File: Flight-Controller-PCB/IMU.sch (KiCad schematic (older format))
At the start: 13 parts, among them Q1 BSS138, Q2 BSS138, U2 ICM-20689

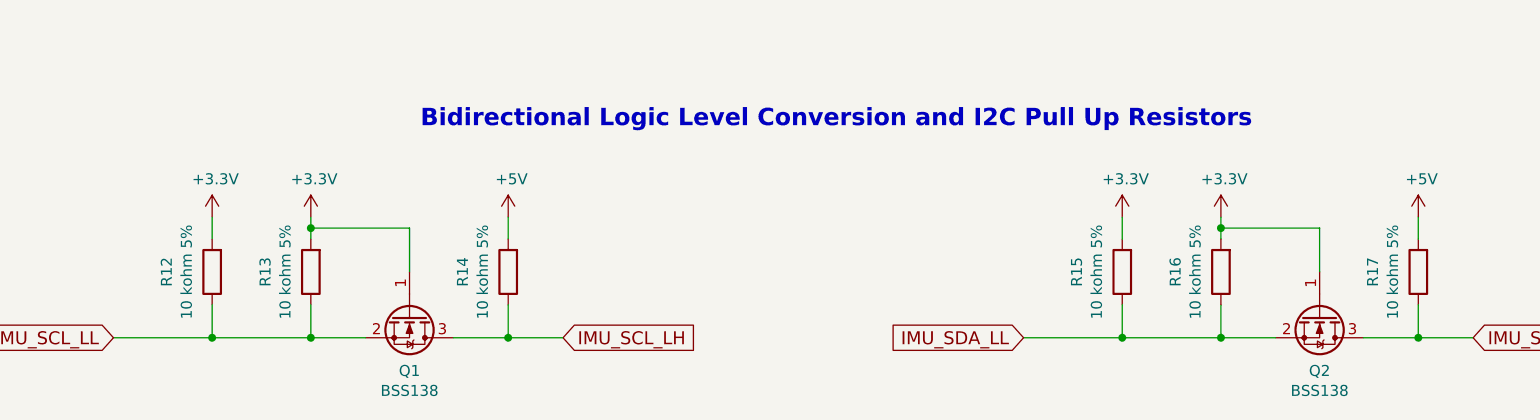
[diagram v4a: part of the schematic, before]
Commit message: Main page and IMU reviewed and passed
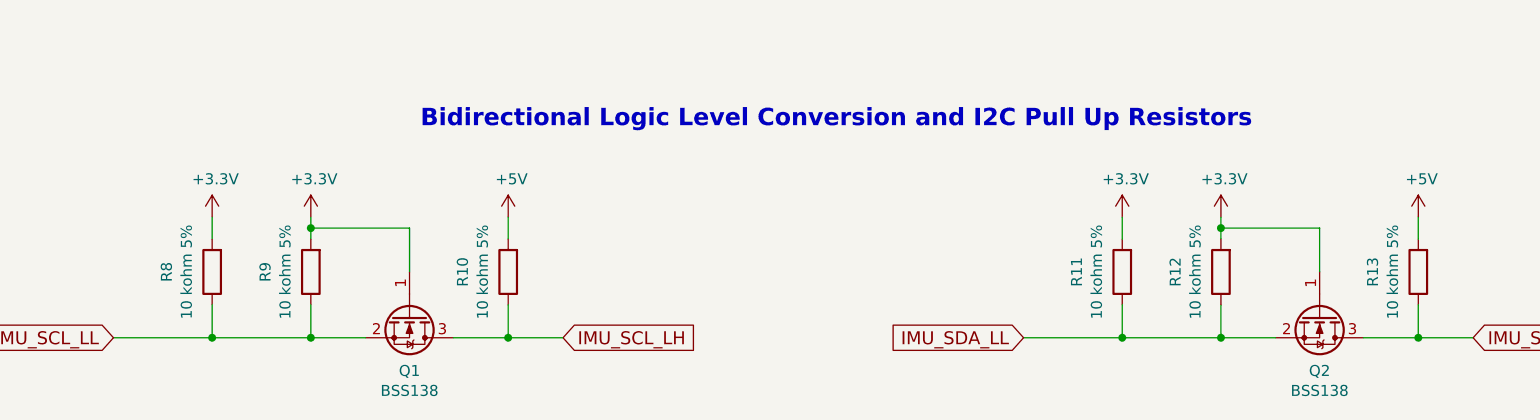
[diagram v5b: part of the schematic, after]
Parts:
- renumbered R14 to R10, R15 to R11, R16 to R12, R17 to R13, R12 to R8, R13 to R9
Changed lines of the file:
@@
 Sheet 2 3
 Title "Six Degree of Freedom (DOF) Inertial Measurement Unit (IMU)"
-Date "2020-12-21"
+Date "2021-01-01"
 Rev "A"
-Comp ""
+Comp "Mark Sherstan"
 Comment1 ""
 Comment2 ""
@@
 IMU_SCL_LL
 $Comp
-L power:+3.3V #PWR030
+L power:+3.3V #PWR034
 U 1 1 5FD9D00C
 P 2800 4700
-AR Path="/5FD99B6C/5FD9D00C" Ref="#PWR030"  Part="1"
+AR Path="/5FD99B6C/5FD9D00C" Ref="#PWR034"  Part="1"
 AR Path="/5FD9E07D/5FD9D00C" Ref="#PWR?"  Part="1"
-F 0 "#PWR030" H 2800 4550 50  0001 C CNN
+F 0 "#PWR034" H 2800 4550 50  0001 C CNN
 F 1 "+3.3V" H 2815 4873 50  0000 C CNN
 F 2 "" H 2800 4700 50  0001 C CNN
@@
 	5050 2800 4750 2800
 $Comp
-L power:GND #PWR035
+L power:GND #PWR039
 U 1 1 5FD9CFF8
 P 4750 3050
-AR Path="/5FD99B6C/5FD9CFF8" Ref="#PWR035"  Part="1"
+AR Path="/5FD99B6C/5FD9CFF8" Ref="#PWR039"  Part="1"
 AR Path="/5FD9E07D/5FD9CFF8" Ref="#PWR?"  Part="1"
-F 0 "#PWR035" H 4750 2800 50  0001 C CNN
+F 0 "#PWR039" H 4750 2800 50  0001 C CNN
 F 1 "GND" H 4755 2877 50  0000 C CNN
 F 2 "" H 4750 3050 50  0001 C CNN
@@
 	3300 2500 3300 3050
 $Comp
-L power:GND #PWR032
+L power:GND #PWR036
 U 1 1 5FD9CFEF
 P 3300 3050
-AR Path="/5FD99B6C/5FD9CFEF" Ref="#PWR032"  Part="1"
+AR Path="/5FD99B6C/5FD9CFEF" Ref="#PWR036"  Part="1"
 AR Path="/5FD9E07D/5FD9CFEF" Ref="#PWR?"  Part="1"
-F 0 "#PWR032" H 3300 2800 50  0001 C CNN
+F 0 "#PWR036" H 3300 2800 50  0001 C CNN
 F 1 "GND" H 3305 2877 50  0000 C CNN
 F 2 "" H 3300 3050 50  0001 C CNN
@@
 	3700 3050 3700 2950
 $Comp
-L power:GND #PWR033
+L power:GND #PWR037
 U 1 1 5FD9CFE8
 P 3700 3050
-AR Path="/5FD99B6C/5FD9CFE8" Ref="#PWR033"  Part="1"
+AR Path="/5FD99B6C/5FD9CFE8" Ref="#PWR037"  Part="1"
 AR Path="/5FD9E07D/5FD9CFE8" Ref="#PWR?"  Part="1"
-F 0 "#PWR033" H 3700 2800 50  0001 C CNN
+F 0 "#PWR037" H 3700 2800 50  0001 C CNN
 F 1 "GND" H 3705 2877 50  0000 C CNN
 F 2 "" H 3700 3050 50  0001 C CNN
@@
 	6050 2500 7050 2500
 $Comp
-L power:GND #PWR041
+L power:GND #PWR045
 U 1 1 5FD9CFD9
 P 8100 3000
-AR Path="/5FD99B6C/5FD9CFD9" Ref="#PWR041"  Part="1"
+AR Path="/5FD99B6C/5FD9CFD9" Ref="#PWR045"  Part="1"
 AR Path="/5FD9E07D/5FD9CFD9" Ref="#PWR?"  Part="1"
-F 0 "#PWR041" H 8100 2750 50  0001 C CNN
+F 0 "#PWR045" H 8100 2750 50  0001 C CNN
 F 1 "GND" H 8105 2827 50  0000 C CNN
 F 2 "" H 8100 3000 50  0001 C CNN
@@
 $EndComp
 $Comp
-L power:GND #PWR038
+L power:GND #PWR042
 U 1 1 5FD9CFD3
 P 7050 3000
-AR Path="/5FD99B6C/5FD9CFD3" Ref="#PWR038"  Part="1"
+AR Path="/5FD99B6C/5FD9CFD3" Ref="#PWR042"  Part="1"
 AR Path="/5FD9E07D/5FD9CFD3" Ref="#PWR?"  Part="1"
-F 0 "#PWR038" H 7050 2750 50  0001 C CNN
+F 0 "#PWR042" H 7050 2750 50  0001 C CNN
 F 1 "GND" H 7055 2827 50  0000 C CNN
 F 2 "" H 7050 3000 50  0001 C CNN
@@
 	6050 2350 6150 2350
 $Comp
-L power:+3.3V #PWR040
+L power:+3.3V #PWR044
 U 1 1 5FD9CFC9
 P 8100 2400
-AR Path="/5FD99B6C/5FD9CFC9" Ref="#PWR040"  Part="1"
+AR Path="/5FD99B6C/5FD9CFC9" Ref="#PWR044"  Part="1"
 AR Path="/5FD9E07D/5FD9CFC9" Ref="#PWR?"  Part="1"
-F 0 "#PWR040" H 8100 2250 50  0001 C CNN
+F 0 "#PWR044" H 8100 2250 50  0001 C CNN
 F 1 "+3.3V" H 8115 2573 50  0000 C CNN
 F 2 "" H 8100 2400 50  0001 C CNN
@@
 	2300 2250 2300 2350
 $Comp
-L power:GND #PWR029
+L power:GND #PWR033
 U 1 1 5FD9CFBF
 P 2300 2850
-AR Path="/5FD99B6C/5FD9CFBF" Ref="#PWR029"  Part="1"
+AR Path="/5FD99B6C/5FD9CFBF" Ref="#PWR033"  Part="1"
 AR Path="/5FD9E07D/5FD9CFBF" Ref="#PWR?"  Part="1"
-F 0 "#PWR029" H 2300 2600 50  0001 C CNN
+F 0 "#PWR033" H 2300 2600 50  0001 C CNN
 F 1 "GND" H 2305 2677 50  0000 C CNN
 F 2 "" H 2300 2850 50  0001 C CNN
@@
 $EndComp
 $Comp
-L power:+3.3V #PWR028
+L power:+3.3V #PWR032
 U 1 1 5FD9CFB9
 P 2300 2250
-AR Path="/5FD99B6C/5FD9CFB9" Ref="#PWR028"  Part="1"
+AR Path="/5FD99B6C/5FD9CFB9" Ref="#PWR032"  Part="1"
 AR Path="/5FD9E07D/5FD9CFB9" Ref="#PWR?"  Part="1"
-F 0 "#PWR028" H 2300 2100 50  0001 C CNN
+F 0 "#PWR032" H 2300 2100 50  0001 C CNN
 F 1 "+3.3V" H 2315 2423 50  0000 C CNN
 F 2 "" H 2300 2250 50  0001 C CNN
@@
 $EndComp
 $Comp
-L Device:R R12
+L Device:R R8
 U 1 1 5FD9CFB3
 P 2800 4950
-AR Path="/5FD99B6C/5FD9CFB3" Ref="R12"  Part="1"
+AR Path="/5FD99B6C/5FD9CFB3" Ref="R8"  Part="1"
 AR Path="/5FD9E07D/5FD9CFB3" Ref="R?"  Part="1"
-F 0 "R12" V 3007 4950 50  0000 C CNN
+F 0 "R8" V 3007 4950 50  0000 C CNN
 F 1 "10 kohm 5%" V 2916 4950 50  0000 C CNN
 F 2 "Resistor_SMD:R_0603_1608Metric_Pad1.05x0.95mm_HandSolder" V 2730 4950 50  0001 C CNN
@@
 $EndComp
 $Comp
-L power:GND #PWR036
+L power:GND #PWR040
 U 1 1 5FD9CFAD
 P 6300 2150
-AR Path="/5FD99B6C/5FD9CFAD" Ref="#PWR036"  Part="1"
+AR Path="/5FD99B6C/5FD9CFAD" Ref="#PWR040"  Part="1"
 AR Path="/5FD9E07D/5FD9CFAD" Ref="#PWR?"  Part="1"
-F 0 "#PWR036" H 6300 1900 50  0001 C CNN
+F 0 "#PWR040" H 6300 1900 50  0001 C CNN
 F 1 "GND" H 6305 1977 50  0000 C CNN
 F 2 "" H 6300 2150 50  0001 C CNN
@@
 $EndComp
 $Comp
-L Device:R R13
+L Device:R R9
 U 1 1 5FDA5523
 P 3250 4950
-AR Path="/5FD99B6C/5FDA5523" Ref="R13"  Part="1"
+AR Path="/5FD99B6C/5FDA5523" Ref="R9"  Part="1"
 AR Path="/5FD9E07D/5FDA5523" Ref="R?"  Part="1"
-F 0 "R13" V 3457 4950 50  0000 C CNN
+F 0 "R9" V 3457 4950 50  0000 C CNN
 F 1 "10 kohm 5%" V 3366 4950 50  0000 C CNN
 F 2 "Resistor_SMD:R_0603_1608Metric_Pad1.05x0.95mm_HandSolder" V 3180 4950 50  0001 C CNN
@@
 $EndComp
 $Comp
-L power:+3.3V #PWR031
+L power:+3.3V #PWR035
 U 1 1 5FDA626A
 P 3250 4700
-AR Path="/5FD99B6C/5FDA626A" Ref="#PWR031"  Part="1"
+AR Path="/5FD99B6C/5FDA626A" Ref="#PWR035"  Part="1"
 AR Path="/5FD9E07D/5FDA626A" Ref="#PWR?"  Part="1"
-F 0 "#PWR031" H 3250 4550 50  0001 C CNN
+F 0 "#PWR035" H 3250 4550 50  0001 C CNN
 F 1 "+3.3V" H 3265 4873 50  0000 C CNN
 F 2 "" H 3250 4700 50  0001 C CNN
@@
 $EndComp
 $Comp
-L Device:R R14
+L Device:R R10
 U 1 1 5FDA6839
 P 4150 4950
-AR Path="/5FD99B6C/5FDA6839" Ref="R14"  Part="1"
+AR Path="/5FD99B6C/5FDA6839" Ref="R10"  Part="1"
 AR Path="/5FD9E07D/5FDA6839" Ref="R?"  Part="1"
-F 0 "R14" V 4357 4950 50  0000 C CNN
+F 0 "R10" V 4357 4950 50  0000 C CNN
 F 1 "10 kohm 5%" V 4266 4950 50  0000 C CNN
 F 2 "Resistor_SMD:R_0603_1608Metric_Pad1.05x0.95mm_HandSolder" V 4080 4950 50  0001 C CNN
@@
 $EndComp
 $Comp
-L power:+5V #PWR034
+L power:+5V #PWR038
 U 1 1 5FDA6B36
 P 4150 4700
-F 0 "#PWR034" H 4150 4550 50  0001 C CNN
+F 0 "#PWR038" H 4150 4550 50  0001 C CNN
 F 1 "+5V" H 4165 4873 50  0000 C CNN
 F 2 "" H 4150 4700 50  0001 C CNN
@@
 	2800 4800 2800 4700
 $Comp
-L power:+3.3V #PWR037
+L power:+3.3V #PWR041
 U 1 1 5FDB9369
 P 6950 4700
-AR Path="/5FD99B6C/5FDB9369" Ref="#PWR037"  Part="1"
+AR Path="/5FD99B6C/5FDB9369" Ref="#PWR041"  Part="1"
 AR Path="/5FD9E07D/5FDB9369" Ref="#PWR?"  Part="1"
-F 0 "#PWR037" H 6950 4550 50  0001 C CNN
+F 0 "#PWR041" H 6950 4550 50  0001 C CNN
 F 1 "+3.3V" H 6965 4873 50  0000 C CNN
 F 2 "" H 6950 4700 50  0001 C CNN
@@
 $EndComp
 $Comp
-L Device:R R15
+L Device:R R11
 U 1 1 5FDB9375
 P 6950 4950
-AR Path="/5FD99B6C/5FDB9375" Ref="R15"  Part="1"
+AR Path="/5FD99B6C/5FDB9375" Ref="R11"  Part="1"
 AR Path="/5FD9E07D/5FDB9375" Ref="R?"  Part="1"
-F 0 "R15" V 7157 4950 50  0000 C CNN
+F 0 "R11" V 7157 4950 50  0000 C CNN
 F 1 "10 kohm 5%" V 7066 4950 50  0000 C CNN
 F 2 "Resistor_SMD:R_0603_1608Metric_Pad1.05x0.95mm_HandSolder" V 6880 4950 50  0001 C CNN
@@
 $EndComp
 $Comp
-L Device:R R16
+L Device:R R12
 U 1 1 5FDB937B
 P 7400 4950
-AR Path="/5FD99B6C/5FDB937B" Ref="R16"  Part="1"
+AR Path="/5FD99B6C/5FDB937B" Ref="R12"  Part="1"
 AR Path="/5FD9E07D/5FDB937B" Ref="R?"  Part="1"
-F 0 "R16" V 7607 4950 50  0000 C CNN
+F 0 "R12" V 7607 4950 50  0000 C CNN
 F 1 "10 kohm 5%" V 7516 4950 50  0000 C CNN
 F 2 "Resistor_SMD:R_0603_1608Metric_Pad1.05x0.95mm_HandSolder" V 7330 4950 50  0001 C CNN
@@
 $EndComp
 $Comp
-L power:+3.3V #PWR039
+L power:+3.3V #PWR043
 U 1 1 5FDB9381
 P 7400 4700
-AR Path="/5FD99B6C/5FDB9381" Ref="#PWR039"  Part="1"
+AR Path="/5FD99B6C/5FDB9381" Ref="#PWR043"  Part="1"
 AR Path="/5FD9E07D/5FDB9381" Ref="#PWR?"  Part="1"
-F 0 "#PWR039" H 7400 4550 50  0001 C CNN
+F 0 "#PWR043" H 7400 4550 50  0001 C CNN
 F 1 "+3.3V" H 7415 4873 50  0000 C CNN
 F 2 "" H 7400 4700 50  0001 C CNN
@@
 $EndComp
 $Comp
-L Device:R R17
+L Device:R R13
 U 1 1 5FDB9387
 P 8300 4950
-AR Path="/5FD99B6C/5FDB9387" Ref="R17"  Part="1"
+AR Path="/5FD99B6C/5FDB9387" Ref="R13"  Part="1"
 AR Path="/5FD9E07D/5FDB9387" Ref="R?"  Part="1"
-F 0 "R17" V 8507 4950 50  0000 C CNN
+F 0 "R13" V 8507 4950 50  0000 C CNN
 F 1 "10 kohm 5%" V 8416 4950 50  0000 C CNN
 F 2 "Resistor_SMD:R_0603_1608Metric_Pad1.05x0.95mm_HandSolder" V 8230 4950 50  0001 C CNN
@@
 $EndComp
 $Comp
-L power:+5V #PWR042
+L power:+5V #PWR046
 U 1 1 5FDB938D
 P 8300 4700
-F 0 "#PWR042" H 8300 4550 50  0001 C CNN
+F 0 "#PWR046" H 8300 4550 50  0001 C CNN
 F 1 "+5V" H 8315 4873 50  0000 C CNN
 F 2 "" H 8300 4700 50  0001 C CNN
